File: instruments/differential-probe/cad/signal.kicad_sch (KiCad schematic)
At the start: 33 parts, among them J3 BNC / panel / 50 R, Q1 MMBT3906,215, SW1 DPDT / ON-ON, U12 OPA810IDR, U3 OPA810IDR, U4 OPA810IDR, U5 TLV1704AIPWR, U6 TLV1702AIDGKR, U7 CD4013BM96

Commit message: wip(instruments): Rev C mirrored HV ladder layout, TL431-free warning, OPA2810 chain
Co-Authored-By: Claude Opus 5.5 <noreply@anthropic.com>
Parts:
- removed R64, R66, R97, R98, R99: 499 R / 0.01%, Resistor_SMD:R_0603_1608Metric, symbol Probe:R_Small_US
- removed U4: OPA810IDR, Package_SO:SOIC-8_3.9x4.9mm_P1.27mm, symbol Probe:OPA810
- J3: value BNC / panel / 50 R -> BNC / PCB right-angle / 50 R; footprint (none) -> Connector_Coaxial:BNC_TEConnectivity_1478035_Horizontal; MPN 31-221-RFX -> 1-1478035-0; Manufacturer Amphenol RF -> TE Connectivity
- R63, R65: value 499 R / 0.01% -> 1.00 kR / 0.01%; MPN RNCF0603TKY499R -> RNCF0603TKY1K00
- R68: value 499 R / 0.01% -> 2.00 kR / 0.01%; MPN RNCF0603TKY499R -> RNCF0603TKY2K00
- SW1: value DPDT / ON-ON -> SPDT / ON-ON / gold; footprint (none) -> Probe:Toggle_SPDT_RightAngle; symbol Probe:DPDT -> Probe:SPDT; MPN 7201SYZBE -> TBD
- U3: value OPA810IDR -> OPA2810IDR; symbol Probe:OPA810 -> Probe:OPA2810; LCSC C1852077 -> C1849413; MPN OPA810IDR -> OPA2810IDR
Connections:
- net REF_N is gone; now on net -4V8: D3.1 (A1)
- net REF_P is gone; now on net +4V8: D3.2 (K2)
- net +4V8: now also U3.8 (V+); no longer U3.7 (V+)
- net DRIVE: now also U3.1 (OUT1), U3.2 (-IN1)
- net FILTER: now also U3.3 (+IN1)
- net FINE_OUT: now also R68.2
- net GND: now also R63.2
- net RAW_OUT: now also R65.2, U3.7 (OUT2); no longer U3.6 (OUT)
- net SUM_N: now also U3.6 (-IN2); no longer U3.2 (-IN)
- net SUM_P: now also U3.5 (+IN2); no longer U3.3 (+IN)
- no-connect marks 15 -> 6
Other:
- note added: "SHARED FILTER / COAX DRIVER (U3 ch 1) / OUTPUT CLAMP"
- note added: "SW1 common (pin 2) selects 1 = 1000:1, 3 = 200:1. No switched feedback. Verify BBM contacts; allow settling during changes."
- note removed: "SHARED FILTER / COAX DRIVER / OUTPUT CLAMP"
- note removed: "SW1 pin 2 selects 1 = 1000:1, 3 = 200:1. No switched feedback. Verify BBM contacts; allow settling during changes."
- moved on the sheet: R68

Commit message: wip(instruments): Rev C PCB-mount edge parts, HV notch shift, LV floorplan
Co-Authored-By: Claude Opus 5.5 <noreply@anthropic.com>
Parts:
- J3: value BNC / PCB right-angle / 50 R -> BNC / PCB right-angle bulkhead / 50 R; footprint Connector_Coaxial:BNC_TEConnectivity_1478035_Horizontal -> Probe:BNC_Amphenol_031-5431_Horizontal; LCSC (none) -> C6956217; MPN 1-1478035-0 -> 031-5431-10RFX; Manufacturer TE Connectivity -> Amphenol RF
- SW1: value SPDT / ON-ON / gold -> SPDT / ON-ON / gold / threaded; footprint Probe:Toggle_SPDT_RightAngle -> Probe:CK_7101_AV2_SPDT; MPN TBD -> 7101SDAV2BE

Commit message: feat(probe): Rev C cost-down: HV12 divider, Yageo C0G, E-Switch toggles, Basic parts
Implements docs/cost-down.md with no layout change (pads, tracks and
courtyards identical to 5b9a9530b):

- HV divider: Uni-Royal HV121WF2004T4E (1 %, 1 W, 3 kV, JLC-stocked)
  replaces Stackpole HVCB2512BDE2M00; DC trim becomes 4.87 k 0.1 % +
  500 ohm (covers 1 % and 0.1 % strings, so HVCB stays a drop-in).
- Yageo CC1812JKNPOEBN330 (33 pF 3 kV NP0) and CC1206FKNPO9BN103
  (10 nF 1 % NP0) replace the KEMET parts.
- E-Switch 100SP1T1B5M7RE / 100DP1T1B1M7QEH replace the C&K toggles;
  footprints renamed ESwitch_100_M7_* from the E-Switch M7 drawing.
- Non-precision positions move to JLC Basic parts; C61 and the 10 uF
  move to stocked equivalents. Extended MPNs placed by JLC: 33 -> 24.
- check.rs: new MPN asserts, 1 %-string trim proof, divider TCR drift,
  1 W rating text with the 2+3 split fault case stated.

Two boards: components $535.81 -> $148.63 (ledger); with JLC fees,
PCB, ~$100 leads and enclosures $866.44 -> $448.20 (validation/cost.txt).

Co-Authored-By: Claude Opus 5.5 <noreply@anthropic.com>
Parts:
- C61: LCSC (none) -> C113826; MPN C0805C181J5GACTU -> CC0805JRNPO9BN181; Manufacturer KEMET -> Yageo
- Q1: value MMBT3906,215 -> MMBT5401; LCSC (none) -> C8326; MPN MMBT3906,215 -> MMBT5401; Manufacturer Nexperia -> CJ (Jiangsu Changjing)
- R100, R101, R102, R70: LCSC (none) -> C17720; MPN RT0805BRD0749R9L -> 0805W8F499JT5E; Manufacturer Yageo -> Uni-Royal
- R103: LCSC (none) -> C17514; MPN RT0805BRD071ML -> 0805W8F1004T5E; Manufacturer Yageo -> Uni-Royal
- R74: LCSC (none) -> C17713; MPN RT0805BRD0747KL -> 0805W8F4702T5E; Manufacturer Yageo -> Uni-Royal
- SW1: footprint Probe:CK_7101_AV2_SPDT -> Probe:ESwitch_100_M7_SPDT; MPN 7101SDAV2BE -> 100SP1T1B5M7RE; Manufacturer C&K -> E-Switch

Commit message: feat(probe): Basic-part output filter, 220 R / 100 pF C0G
F3 of docs/fee-consolidation.md. R69 97.6 R RC0805FR becomes the
on-board Uni-Royal 0805W8F2200T5E and C61 180 pF CC0805JRNPO9BN181
becomes Samsung CL21C101JBANNNC (100 pF C0G 5 % 50 V, LCSC C1790,
Basic). Same 0805 footprints, no layout change. Pole 6.000 -> 5.900 MHz;
vendor model -3 dB 5.786 -> 5.628 MHz wide, 5.252 -> 5.131 MHz fine, no
peaking; 60 kHz phase -0.938 -> -0.953 deg wide. Strategy E: 23 -> 21
Extended, fees $81.09 -> $74.95, board total $248.02 -> $241.85.

Co-Authored-By: Claude Opus 5.5 <noreply@anthropic.com>
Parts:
- C61: value 180 pF -> 100 pF; LCSC C113826 -> C1790; MPN CC0805JRNPO9BN181 -> CL21C101JBANNNC; Manufacturer Yageo -> Samsung Electro-Mechanics
- R69: value 97.6 R / 1% -> 220 R; LCSC C483266 -> C17557; MPN RC0805FR-0797R6L -> 0805W8F2200T5E; Manufacturer YAGEO -> Uni-Royal

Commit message: feat(probe): two-pole output filter with bandwidth jumper (C61 47 pF, C62 330 pF, JP1)
C61 drops to 47 pF C0G (CL21C470JBANNNC, Basic) and C62 330 pF C0G
(CL10C331JB8NNNC, Basic) shunts OUT at the BNC through the bridged
solder jumper JP1 (KiCad net-tie footprint, PCB copper, not in the BOM).
Cutting JP1 gives the ~11 MHz mode.

Vendor model (validation/spice/results.txt, interpolated): 5.768 MHz
wide / 5.273 MHz fine, no peaking, 60 kHz phase -1.000 / -1.241 deg;
JP1 cut 10.856 / 8.471 MHz. Full-band input-referred noise 172 / 116 mV
(was 373 / 141; tools/output_filter_study.py). The finding: U3A's
unfiltered tail dominated full-band noise (ideal U3A: 373 -> 157 mV).

ac.cir carries the JP1-cut case as a second run; candidates.cir keeps the
historical single-pole cases with JP=0. cost.py gains a feature layer
(FEATURE_SUBS/ADDS) and strategy H; +$0.20 two boards, no new Extended.
Gates: make check, pcb-check (DRC 0/0), pcb-oracle, simulate, export.sh.

Co-Authored-By: Claude Opus 5.5 <noreply@anthropic.com>
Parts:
- added C62: 330 pF, Capacitor_SMD:C_0603_1608Metric, symbol Probe:C
- added JP1: BW / bridged = 5.8 MHz, cut = 11 MHz, Jumper:SolderJumper-2_P1.3mm_Bridged_RoundedPad1.0x1.5mm, symbol Probe:SolderJumper_2_Bridged
- C61: value 100 pF -> 47 pF; LCSC C1790 -> C14857; MPN CL21C101JBANNNC -> CL21C470JBANNNC
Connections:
- net GND: now also C62.2
- net OUT: now also JP1.1 (A)
- new net OUT_C: C62.1, JP1.2 (B)

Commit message: feat(probe): latched overvoltage trigger output on a second BNC (J4)
CD4013 flip-flop 2 (pins 8/10 on SET/RESET, /Q2 = TRIG_DRV) latches with
the warning LED and drives Q3 (MMBT5401) high-side through R110 22k
(0805W8F2202T5E, Basic); R112 470R (0805W8F4700T5E, Basic) feeds J4,
R111 10k holds 0 V idle, D10 BAV199 clamps TRIG_C. J4 cannot reach the
latch or comparators.

check.rs (worst-case rails/resistors): 4.445-4.920 V into 1 Mohm,
0.418-0.484 V into 50 ohm; Q3 forced beta <= 31 at the 11.1 mA short;
R112 <= 54 mW shorted; tolerated drive -7.5..+11.4 V. Latency estimate
1.64 us after OV_N (assumed Ceb 30 pF, 25 C maxima), plus TLV1704
460 ns typ: an estimate, not a bound, and not a peak-capture guarantee.

Panel order J4 7.72, SW1 21.36, J3 35.0, SW2 56.0; H1 moved to
(131.0, 31.2). LV top fill 33.0 -> 37.0 %. Cost +$7.42 two boards
(H - E now +$7.61), Extended 20 -> 20.
Gates: make check, pcb-check (DRC 0/0), pcb-oracle, simulate, export.sh.

Co-Authored-By: Claude Opus 5.5 <noreply@anthropic.com>
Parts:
- added D10: BAV199,215, Package_TO_SOT_SMD:SOT-23, symbol Probe:BAV199
- added J4: BNC / PCB right-angle bulkhead / 50 R, Probe:BNC_Amphenol_031-5431_Horizontal, symbol Probe:BNC
- added Q3: MMBT5401, Package_TO_SOT_SMD:SOT-23, symbol Probe:PNP
- added R110: 22 kR, Resistor_SMD:R_0805_2012Metric, symbol Probe:R_Small_US
- added R111: 10 kR, Resistor_SMD:R_0805_2012Metric, symbol Probe:R_Small_US
- added R112: 470 R, Resistor_SMD:R_0805_2012Metric, symbol Probe:R_Small_US
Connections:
- net +4V8: now also D10.2 (K2), Q3.2 (E); no longer U7.10 (RESET2)
- net -4V8: no longer U7.8 (SET2)
- net GND: now also D10.1 (A1), J4.2, R111.2
- net RESET: now also U7.10 (RESET2)
- net SET: now also U7.8 (SET2)
- net TRIG_DRV: now reaches U7.12 (/Q2)
- net TRIG_DRV: now also R110.1
- new net TRIG: J4.1, R112.2
- new net TRIG_B: Q3.1 (B), R110.2
- new net TRIG_C: D10.3 (K1/A2), Q3.3 (C), R111.1, R112.1
- no-connect marks 6 -> 5
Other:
- note added: "OVERVOLTAGE TRIGGER OUTPUT (J4) / latched, 0 V idle, ~4.7 V on 1 MR"
- note added: "Scope trigger, not a peak-capture guarantee. Edge <= 1.35 us after the comparator output (validation/checks.txt)."

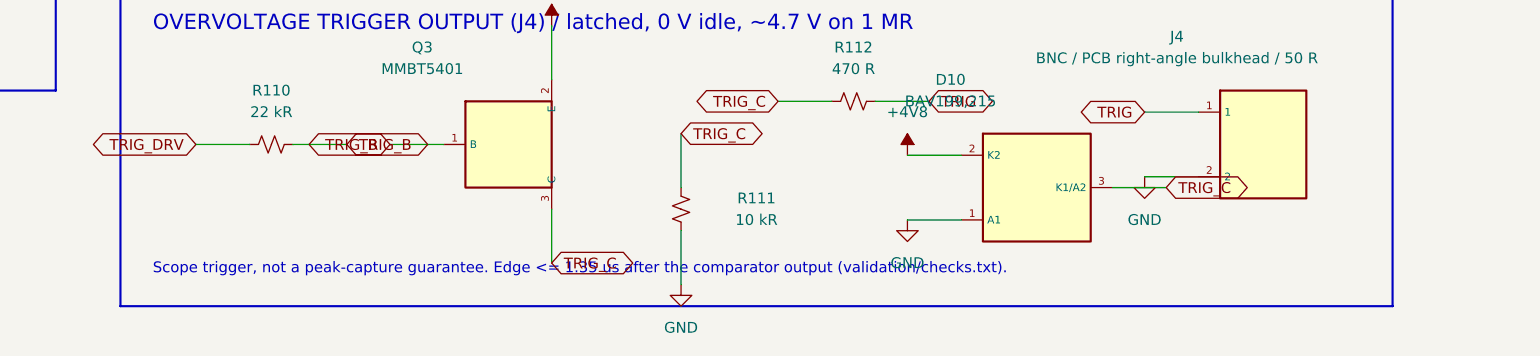
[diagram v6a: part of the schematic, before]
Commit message: fix(probe): trigger schematic note gives the latency estimate, not a bound
The J4 block note still said 'Edge <= 1.35 us'; checks.txt and design.md
give a 1.64 us charge-control estimate that is explicitly not a bound.
Schematic text only; ERC 0, make check passes.

Co-Authored-By: Claude Opus 5.5 <noreply@anthropic.com>
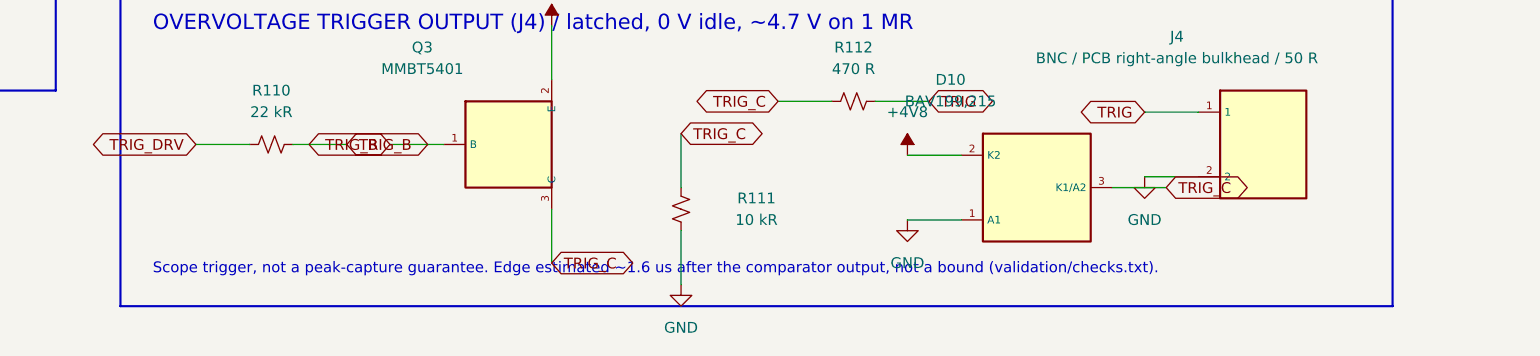
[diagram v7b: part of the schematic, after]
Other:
- note added: "Scope trigger, not a peak-capture guarantee. Edge estimated ~1.6 us after the comparator output, not a bound (validation/checks.txt)."
- note removed: "Scope trigger, not a peak-capture guarantee. Edge <= 1.35 us after the comparator output (validation/checks.txt)."
